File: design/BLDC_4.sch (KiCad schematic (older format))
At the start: 26 parts, among them K1 SERVO, P1 HALL/Encoder, P101 CANBUS, P3 PWR_COMM, P4 IN+, P5 IN-, P6 MOTOR1, P7 MOTOR2, P9 MOTOR3, X1 MINI-USB-SHIELD-32005-201

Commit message: Saved project with more recent version of KiCad. Added IRS2184 half bridge driver to BLDC_4_cache.lib
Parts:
- C2, C3: symbol C -> C-RESCUE-BLDC_4
- D1, D2, D3: symbol LED -> LED-RESCUE-BLDC_4
- R103, R104, R22, R3, R37, R38, R4, R5, R6: symbol R -> R-RESCUE-BLDC_4
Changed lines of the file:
@@
 EESchema Schematic File Version 2
+LIBS:BLDC_4-rescue
 LIBS:power
 LIBS:device
@@
 LIBS:crf_1
 LIBS:BLDC_4-cache
-EELAYER 24 0
+EELAYER 25 0
 EELAYER END
 $Descr A4 11693 8268
@@
 $EndComp
 $Comp
-L GND #PWR02
+L GND-RESCUE-BLDC_4 #PWR02
 U 1 1 522DA053
 P 1500 4400
@@
 $EndComp
 $Comp
-L C C3
+L C-RESCUE-BLDC_4 C3
 U 1 1 522DA0A7
 P 6550 5750
@@
 $EndComp
 $Comp
-L R R5
+L R-RESCUE-BLDC_4 R5
 U 1 1 522DA0AD
 P 6600 5550
@@
 $EndComp
 $Comp
-L C C2
+L C-RESCUE-BLDC_4 C2
 U 1 1 522DA0B3
 P 2050 2400
@@
 $EndComp
 $Comp
-L GND #PWR03
+L GND-RESCUE-BLDC_4 #PWR03
 U 1 1 522DA0BA
 P 7000 5850
@@
 V_SUPPLY
 $Comp
-L GND #PWR04
+L GND-RESCUE-BLDC_4 #PWR04
 U 1 1 522DA0CE
 P 1700 2500
@@
 $EndComp
 $Comp
-L R R4
+L R-RESCUE-BLDC_4 R4
 U 1 1 522DA0D4
 P 2050 2250
@@
 $EndComp
 $Comp
-L R R3
+L R-RESCUE-BLDC_4 R3
 U 1 1 522DA0DA
 P 2050 2150
@@
 $EndComp
 $Comp
-L GND #PWR05
+L GND-RESCUE-BLDC_4 #PWR05
 U 1 1 522DA0E2
 P 1450 5450
@@
 $EndComp
 $Comp
-L GND #PWR06
+L GND-RESCUE-BLDC_4 #PWR06
 U 1 1 522DA0FC
 P 1600 3450
@@
 100R if used as\nservo output
 $Comp
-L R R6
+L R-RESCUE-BLDC_4 R6
 U 1 1 522DA24E
 P 2400 2950
@@
 $EndComp
 $Comp
-L GND #PWR011
+L GND-RESCUE-BLDC_4 #PWR011
 U 1 1 53FA1F8F
 P 9550 5050
@@
 $EndSheet
 $Comp
-L GND #PWR012
+L GND-RESCUE-BLDC_4 #PWR012
 U 1 1 53FB6DA8
 P 1450 4050
@@
 $EndSheet
 $Comp
-L R R103
+L R-RESCUE-BLDC_4 R103
 U 1 1 53FCA251
 P 2400 3050
@@
 $EndComp
 $Comp
-L R R104
+L R-RESCUE-BLDC_4 R104
 U 1 1 53FCA272
 P 2400 3150
@@
 Voltage supply (0 - 60v)\nNeeds external decoupling\ncaps to avoid high voltage\ntransients produced by the\ninductance of the battery\nwiring while switching the FETs\nAlso critical for EMI/RF compliance
 $Comp
-L R R38
+L R-RESCUE-BLDC_4 R38
 U 1 1 53FC020B
 P 5900 6400
@@
 $EndComp
 $Comp
-L LED D2
+L LED-RESCUE-BLDC_4 D2
 U 1 1 53FC0212
 P 5900 6850
@@
 $EndComp
 $Comp
-L GND #PWR013
+L GND-RESCUE-BLDC_4 #PWR013
 U 1 1 53FC021C
 P 5900 7050
@@
 $EndComp
 $Comp
-L R R37
+L R-RESCUE-BLDC_4 R37
 U 1 1 53FC130C
 P 6200 6400
@@
 $EndComp
 $Comp
-L LED D1
+L LED-RESCUE-BLDC_4 D1
 U 1 1 53FC1313
 P 6200 6850
@@
 $EndComp
 $Comp
-L GND #PWR014
+L GND-RESCUE-BLDC_4 #PWR014
 U 1 1 53FC131A
 P 6200 7050
@@
 $EndComp
 $Comp
-L LED D3
+L LED-RESCUE-BLDC_4 D3
 U 1 1 53FC6A60
 P 6500 6850
@@
 $EndComp
 $Comp
-L R R22
+L R-RESCUE-BLDC_4 R22
 U 1 1 53FC6A67
 P 6500 6400
@@
 $EndComp
 $Comp
-L GND #PWR015
+L GND-RESCUE-BLDC_4 #PWR015
 U 1 1 53FC8AA4
 P 6500 7050
@@
 $EndComp
 $Comp
-L GND #PWR018
+L GND-RESCUE-BLDC_4 #PWR018
 U 1 1 548F24DF
 P 9850 5050
@@
 $EndComp
 $Comp
-L GND #PWR019
+L GND-RESCUE-BLDC_4 #PWR019
 U 1 1 548F2504
 P 8450 5100
@@
 $EndComp
 $Comp
-L GND #PWR020
+L GND-RESCUE-BLDC_4 #PWR020
 U 1 1 548F2529
 P 8150 4600
@@
 $EndComp
 $Comp
-L GND #PWR021
+L GND-RESCUE-BLDC_4 #PWR021
 U 1 1 548F254E
 P 8300 4100
@@
 $EndComp
 $Comp
-L GND #PWR022
+L GND-RESCUE-BLDC_4 #PWR022
 U 1 1 548F2573
 P 9100 1500

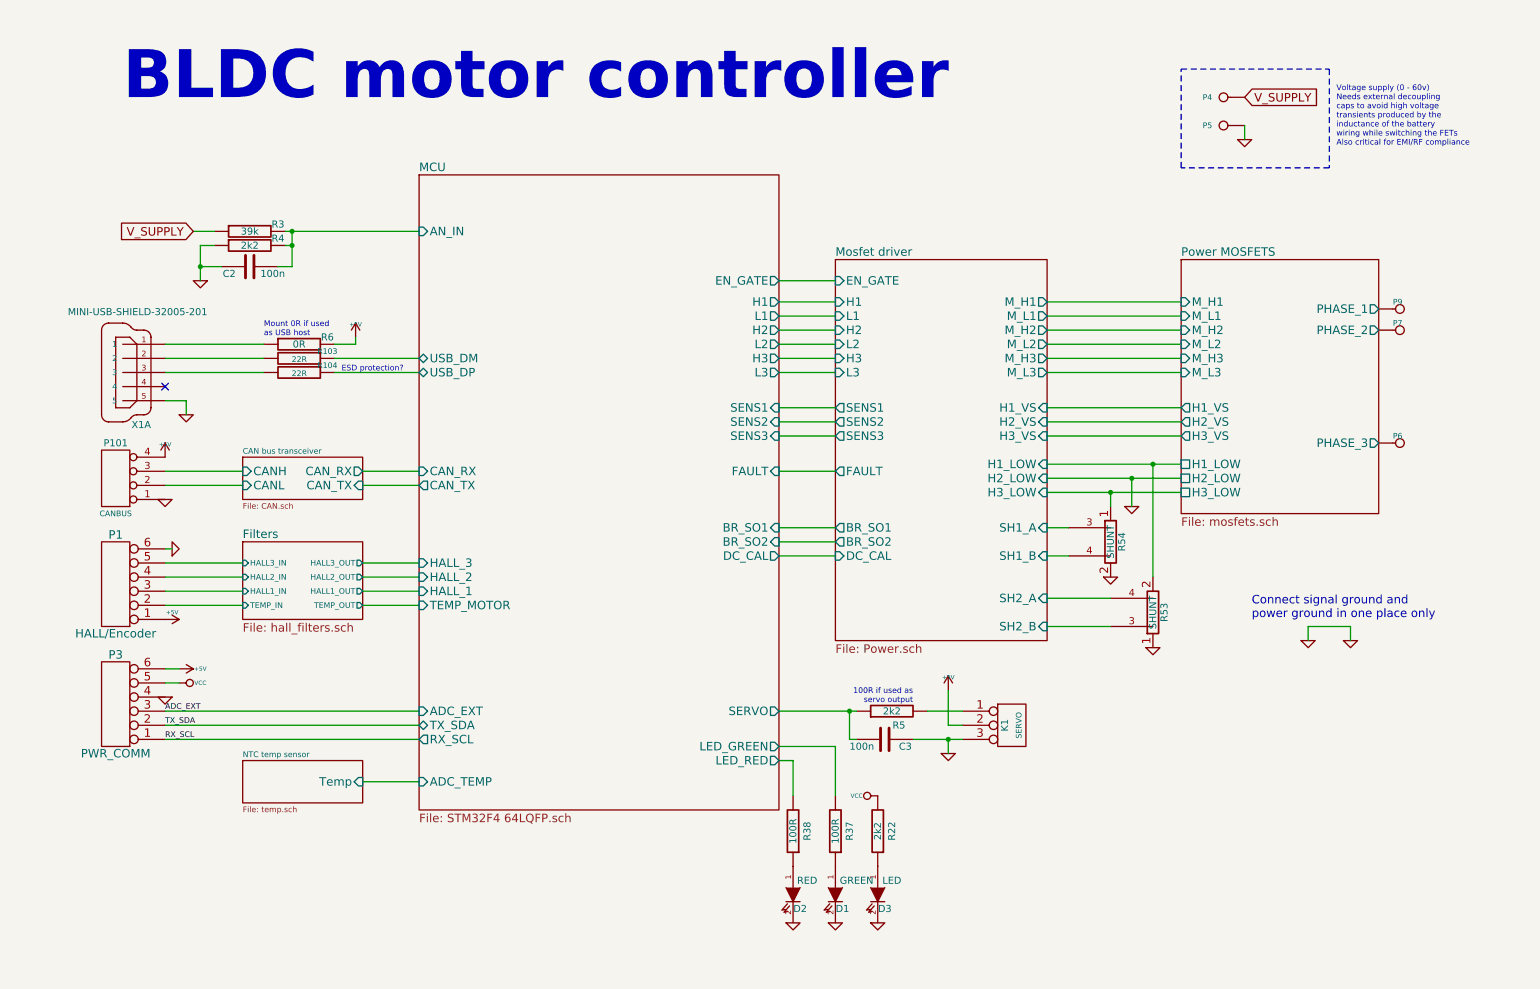
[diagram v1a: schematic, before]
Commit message: Draft IRS2184 bootstrap driver circuit.
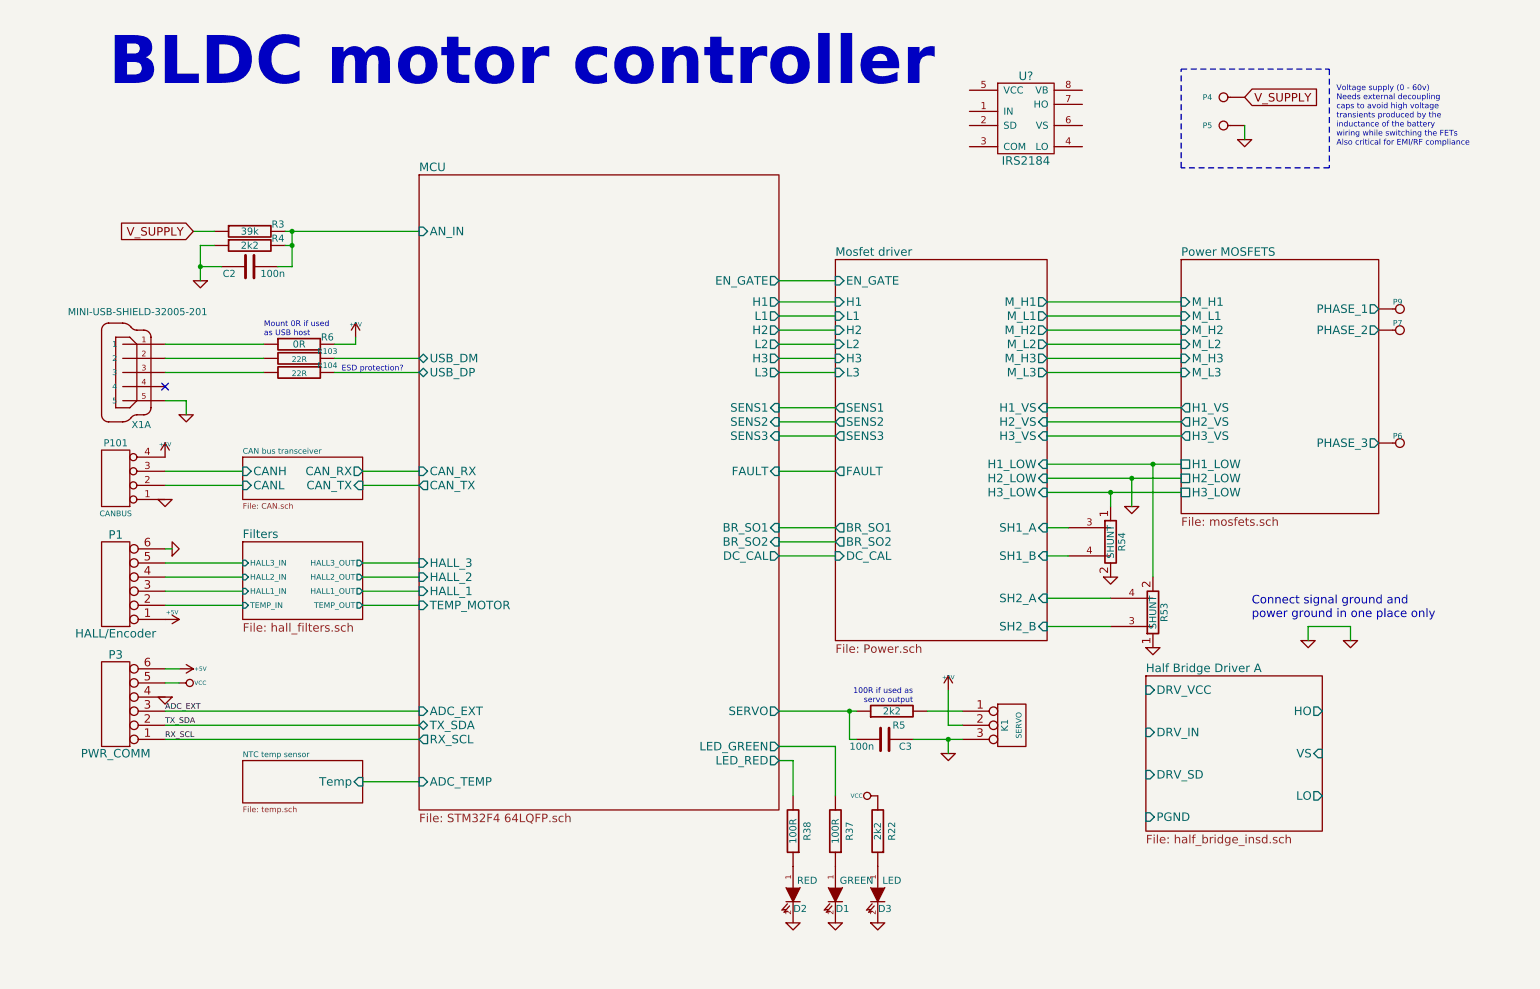
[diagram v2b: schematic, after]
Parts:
- added U?: IRS2184, symbol IRS2184
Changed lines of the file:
@@
 $Descr A4 11693 8268
 encoding utf-8
-Sheet 1 7
+Sheet 1 8
 Title "BLDC Driver 4.6"
 Date "25 Aug 2014"
@@
 Text Label 1450 5550 0    40   ~ 0
 ADC_EXT
-Text Notes 1150 1250 0    340  ~ 68
+Text Notes 1050 1150 0    340  ~ 68
 BLDC motor controller
 $Bitmap
@@
 Text Notes 9150 4900 0    60   ~ 0
 Connect signal ground and\npower ground in one place only
+$Comp
+L IRS2184 U?
+U 1 1 55DB3300
+P 7550 1350
+F 0 "U?" H 7550 1650 60  0000 C CNN
+F 1 "IRS2184" H 7550 1050 60  0000 C CNN
+F 2 "" H 7550 1350 60  0000 C CNN
+F 3 "" H 7550 1350 60  0000 C CNN
+	1    7550 1350
+	1    0    0    -1
+$EndComp
+$Sheet
+S 8400 5300 1250 1100
+U 55DB7E47
+F0 "Half Bridge Driver A" 60
+F1 "half_bridge_insd.sch" 60
+F2 "HO" O R 9650 5550 60
+F3 "LO" O R 9650 6150 60
+F4 "VS" I R 9650 5850 60
+F5 "DRV_VCC" I L 8400 5400 60
+F6 "DRV_IN" I L 8400 5700 60
+F7 "DRV_SD" I L 8400 6000 60
+F8 "PGND" I L 8400 6300 60
+$EndSheet
 $EndSCHEMATC

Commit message: Added new drivers and removed the big old one.
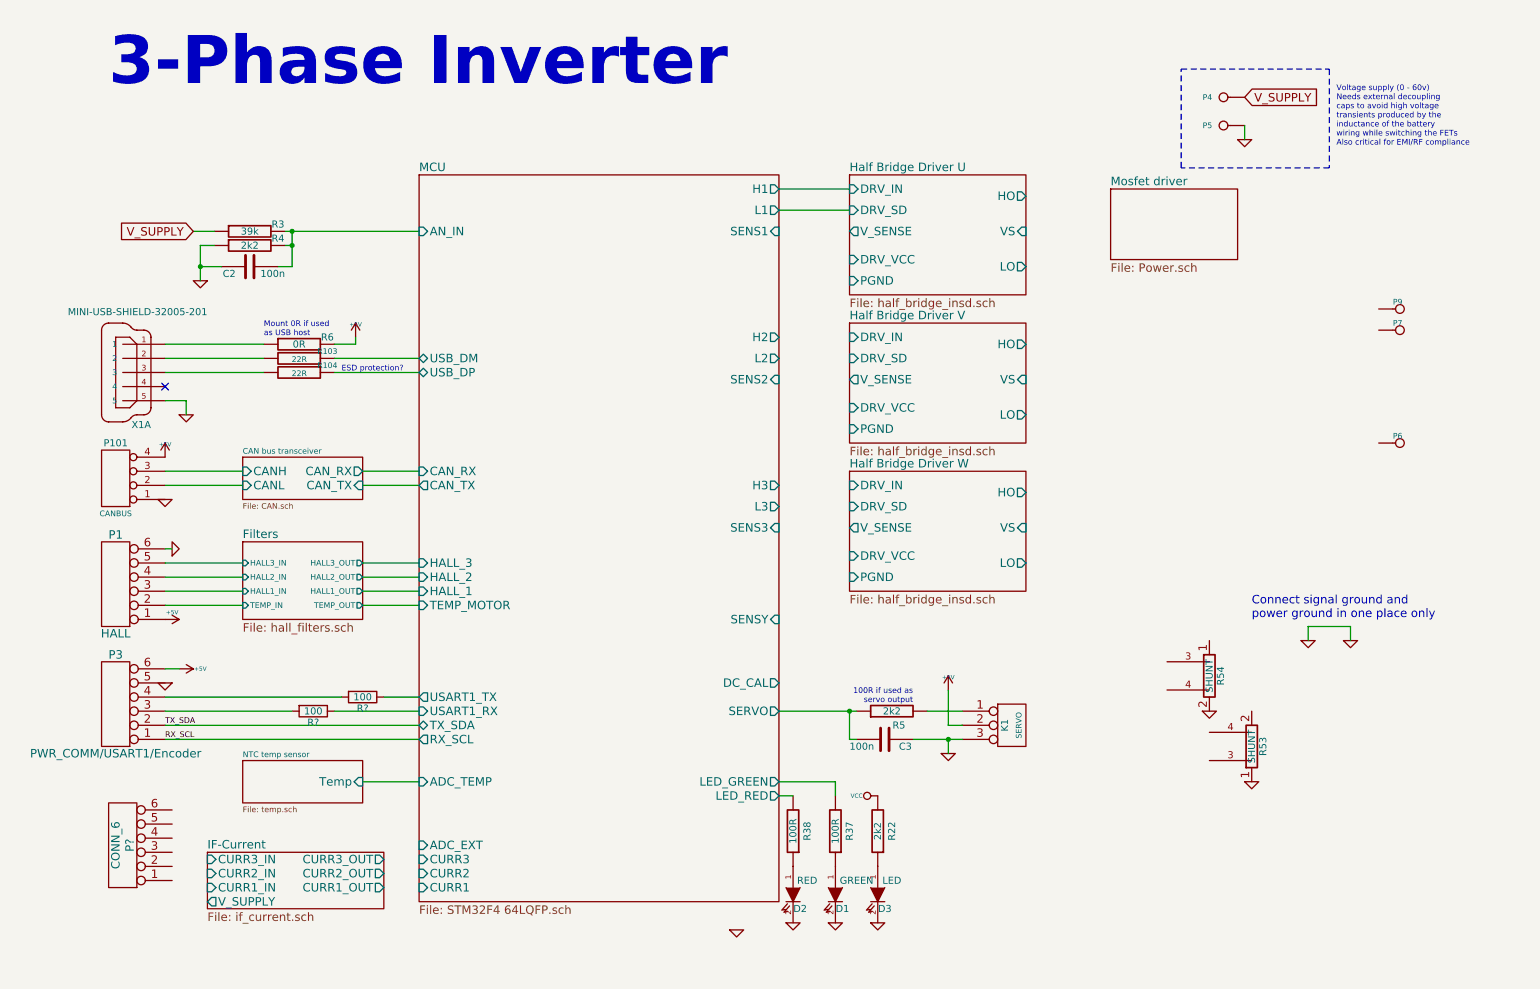
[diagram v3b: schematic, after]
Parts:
- removed U?: IRS2184, symbol IRS2184
- added P?: CONN_6, symbol CONN_6
- added R? (x2): 100, symbol R
- P1: value HALL/Encoder -> HALL
- P3: value PWR_COMM -> PWR_COMM/USART1/Encoder
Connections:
- net GND: now also P3.5; no longer P3.4
- net VCC: no longer P3.5
- net ADC_EXT: no longer names the net of P3.3
- net ADC_EXT: now also R?.2
- net Mosfet driver/H1_LOW: no longer names the net of R53.2
- net Mosfet driver/H3_LOW: no longer names the net of R54.1
- net Mosfet driver/SH1_A: no longer names the net of R54.3
- net Mosfet driver/SH1_B: no longer names the net of R54.4
- net Mosfet driver/SH2_A: no longer names the net of R53.4
- net Mosfet driver/SH2_B: no longer names the net of R53.3
- net Power MOSFETS/PHASE_1: no longer names the net of P9.1
- net Power MOSFETS/PHASE_2: no longer names the net of P7.1
- net Power MOSFETS/PHASE_3: no longer names the net of P6.1
- new net: P3.4, R?.2
- new net MCU/USART1_RX: R?.1
- new net MCU/USART1_TX: R?.1
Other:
- note added: "3-Phase Inverter"
- note removed: "BLDC motor controller"
- moved on the sheet: R53, R54
